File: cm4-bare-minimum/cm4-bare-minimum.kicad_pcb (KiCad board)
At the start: 2 copper layers, 120 x 40 mm, 24 parts, among them J1 Micro_SD_Card_Det, J2 690-019-298-412, J3 THD-02-R, J4 USB4105-GF-A, J5 USB_OTG, U1 RT9742GGJ5, U2 RT9742SNGV, U3 FSUSB42MUX, U5 MagJack-A70-112-331N126

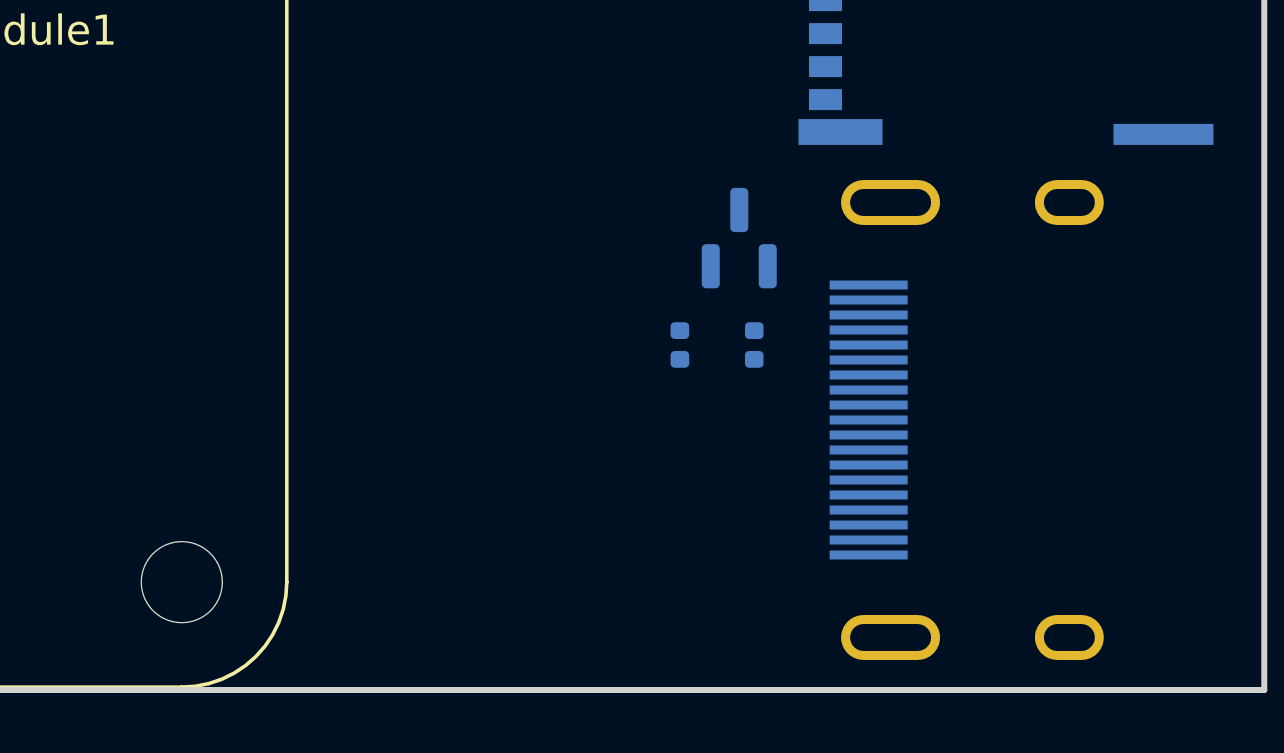
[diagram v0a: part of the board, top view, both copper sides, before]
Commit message: Connector changed, Added Labels.
Changed HDMI connector to upright. Added labels for included components in schematic.
To Do: Create tracks in PCB Layout. Add jumper for wifi bluetooth signals.
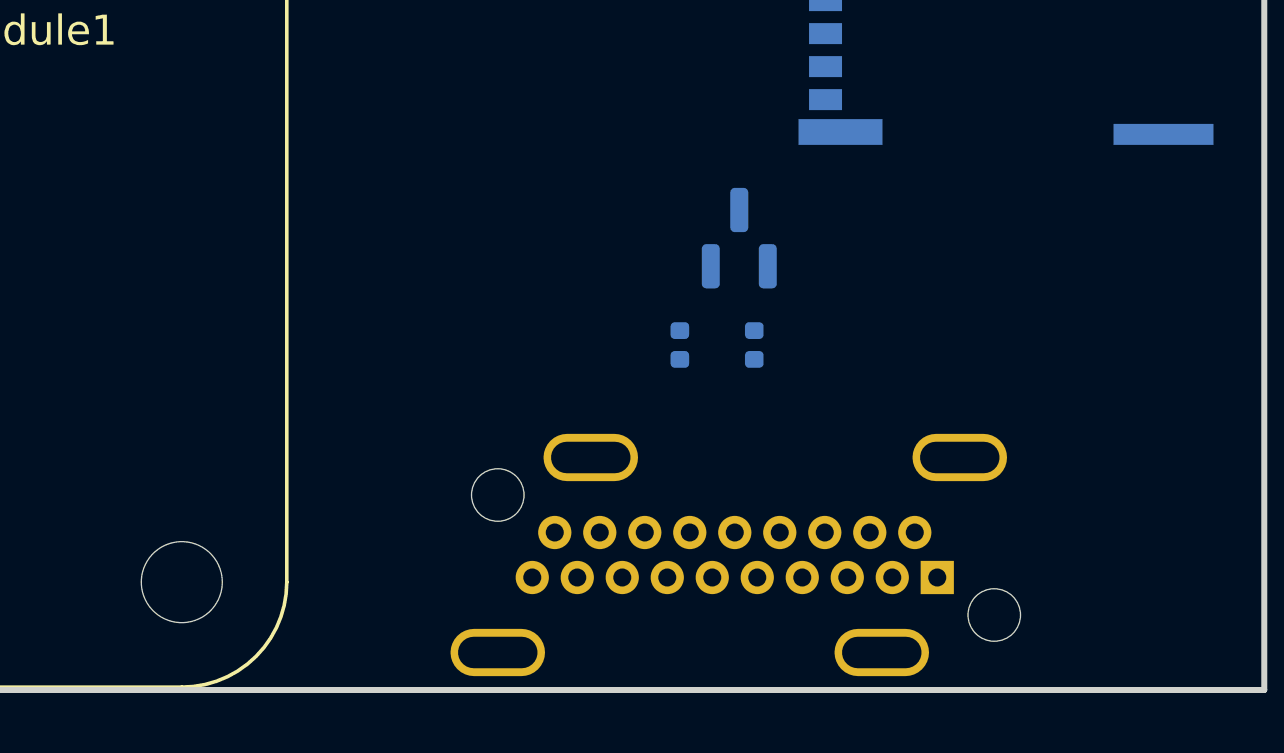
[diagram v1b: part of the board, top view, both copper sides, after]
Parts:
- removed J2: 690-019-298-412, CM4IO:EDAC 690-019-298-412
- added J6: G45A19170083HR, G45A19170083HR:AMPHENOL_G45A19170083HR, B.Cu at (201.5, 115.0)

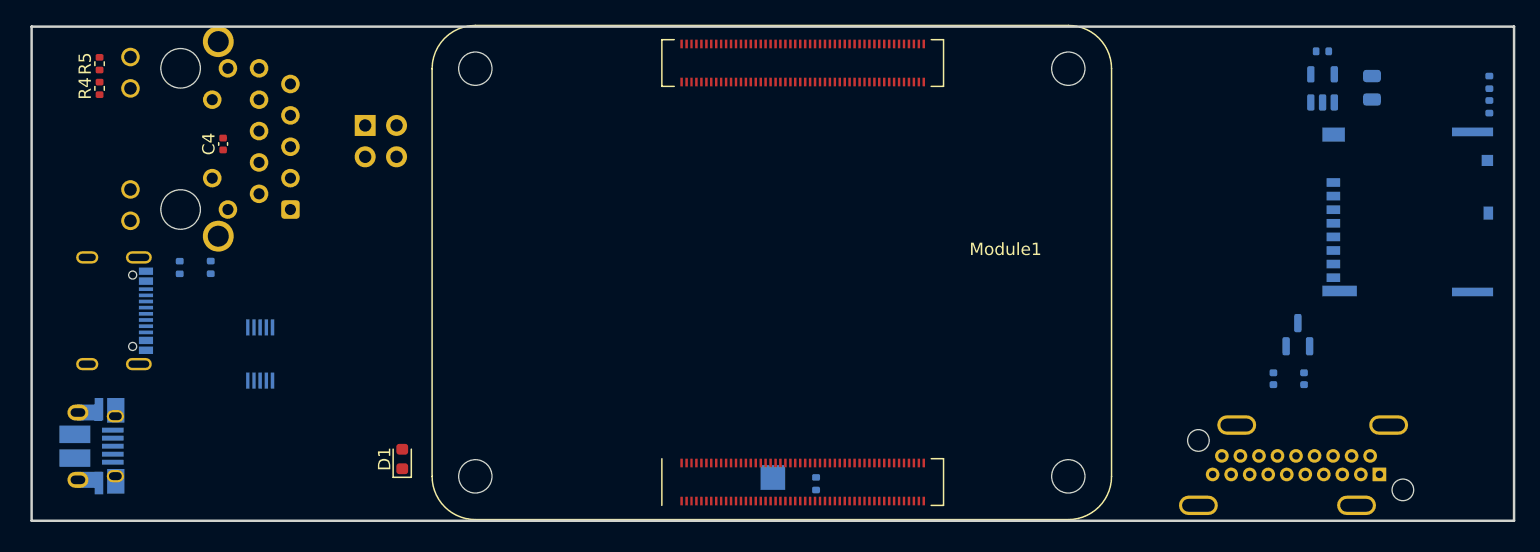
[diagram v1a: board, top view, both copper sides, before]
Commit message: updated V1 bare minimum board
Initiated pcb layout for V1 board
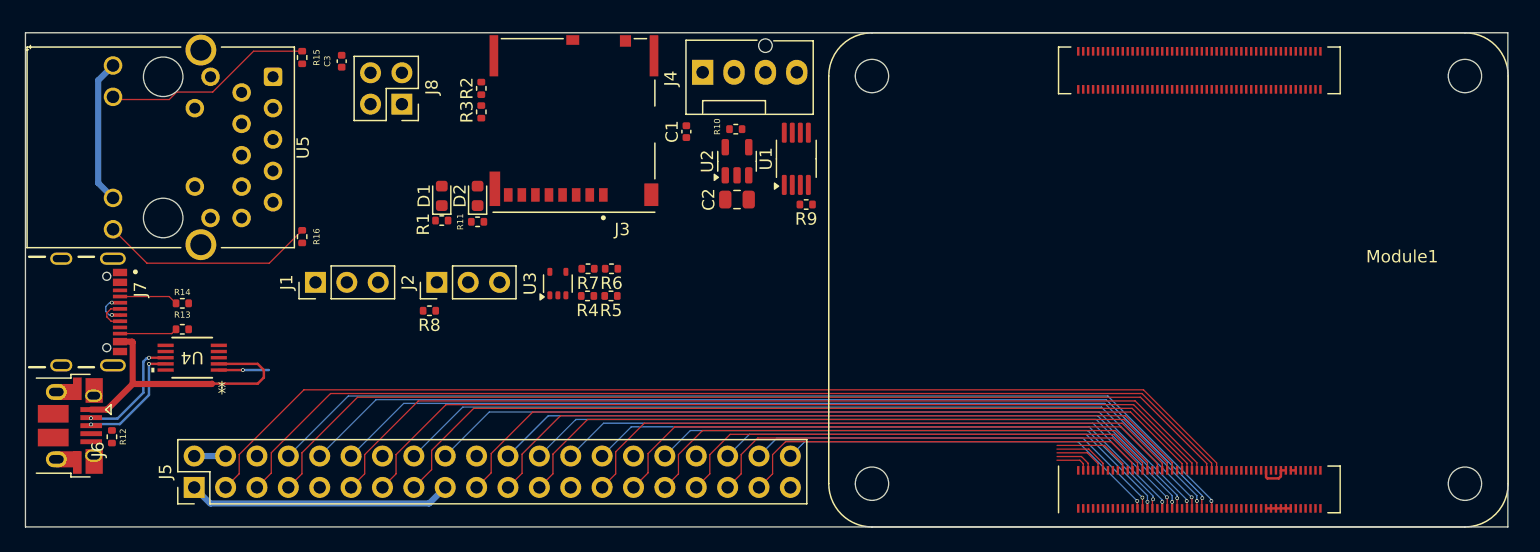
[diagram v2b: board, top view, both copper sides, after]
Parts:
- removed C4: 100n, Capacitor_SMD:C_0402_1005Metric
- removed TP1: TestPoint, TestPoint:TestPoint_Pad_2.0x2.0mm
- added D2: LED Red, LED_SMD:LED_0603_1608Metric, F.Cu at (126.6, 93.2)
- added J2: Conn_01x03, Connector_PinHeader_2.54mm:PinHeader_1x03_P2.54mm_Vertical, F.Cu at (123.3, 100.2)
- added J7: USB4105-GF-A, USB4105-GF-A:GCT_USB4105-GF-A, F.Cu at (92.9, 102.6)
- added J8: THD-02-R, Connector_PinHeader_2.54mm:PinHeader_2x02_P2.54mm_Vertical, F.Cu at (120.5, 85.8)
- added R10: 12K 1%, Resistor_SMD:R_0402_1005Metric, F.Cu at (147.5, 87.8)
- added R11: 1k, Resistor_SMD:R_0402_1005Metric, F.Cu at (126.6, 95.3)
- added R12: 2.2K 1%, Resistor_SMD:R_0402_1005Metric, F.Cu at (97.0, 112.7)
- added R13: 5.1k, Resistor_SMD:R_0402_1005Metric, F.Cu at (102.7, 104.0)
- added R14: 5.1k, Resistor_SMD:R_0402_1005Metric, F.Cu at (102.7, 101.9)
- added R15: 470R, Resistor_SMD:R_0402_1005Metric, F.Cu at (112.4, 82.0)
- added R16: 470R, Resistor_SMD:R_0402_1005Metric, F.Cu at (112.4, 96.5)
- added R9: 36K 1%, Resistor_SMD:R_0402_1005Metric, F.Cu at (153.2, 93.9)
- added U4: FSUSB42MUX, FSUSB42MUX:MSOP10_3X3_ONS, F.Cu at (103.5, 106.3)
- C1: value 10u -> 100n; footprint Capacitor_SMD:C_0805_2012Metric -> Capacitor_SMD:C_0402_1005Metric; moved to F.Cu
- C2: value 100n -> 10u; footprint Capacitor_SMD:C_0402_1005Metric -> Capacitor_SMD:C_0805_2012Metric; moved to F.Cu
- C3, U5: moved to F.Cu
- J1: value Micro_SD_Card_Det -> Conn_01x03; footprint CM4IO:SDCARD_MOLEX_503398-1892 -> Connector_PinHeader_2.54mm:PinHeader_1x03_P2.54mm_Vertical; moved to F.Cu
- J3: value THD-02-R -> Micro_SD_Card_Det; footprint Connector_PinHeader_2.54mm:PinHeader_2x02_P2.54mm_Vertical -> CM4IO:SDCARD_MOLEX_503398-1892; moved to F.Cu
- J4: value USB4105-GF-A -> Molex 470531000; footprint USB4105-GF-A:GCT_USB4105-GF-A -> Connector:FanPinHeader_1x04_P2.54mm_Vertical; moved to F.Cu
- J5: value USB_OTG -> THD-20-R; footprint CM4IO:USB_Micro-B_EDAC_UCON00686 -> Connector_PinHeader_2.54mm:PinHeader_2x20_P2.54mm_Vertical; moved to F.Cu
- J6: value G45A19170083HR -> USB_OTG; footprint G45A19170083HR:AMPHENOL_G45A19170083HR -> CM4IO:USB_Micro-B_EDAC_UCON00686; moved to F.Cu
- R1: value nf -> 1k; moved to F.Cu
- R2: value nf -> NC; moved to F.Cu
- R3: value 12K 1% -> NC; moved to F.Cu
- R4, R5: value 470R -> NC
- R6: value 1k -> NC; moved to F.Cu
- R7: value 2.2K 1% -> NC; moved to F.Cu
- R8: value 5.1k -> NC; moved to F.Cu
- U1: value RT9742GGJ5 -> EMC2301-1-ACZL-TR; footprint Package_TO_SOT_SMD:SOT-23-5 -> Package_SO:MSOP-8_3x3mm_P0.65mm; moved to F.Cu
- U2: value RT9742SNGV -> RT9742GGJ5; footprint Package_TO_SOT_SMD:SOT-23 -> Package_TO_SOT_SMD:SOT-23-5; moved to F.Cu
- U3: value FSUSB42MUX -> 74LVC1G07SE-7; footprint FSUSB42MUX:MSOP10_3X3_ONS -> Package_TO_SOT_SMD:SOT-353_SC-70-5; moved to F.Cu
- moved J6 109.0 mm to (92.5, 111.8)
- moved J1 88.2 mm to (113.5, 100.2), turned to 90 degrees
- moved R1 85.5 mm to (123.7, 95.2), turned to 0 degrees
- moved R2 81.6 mm to (126.9, 84.5)
- moved C3 79.7 mm to (115.6, 82.3)
- moved R3 68.3 mm to (126.9, 86.4), turned to 90 degrees
- moved C1 55.6 mm to (143.5, 88.0)
- moved J4 53.4 mm to (144.8, 83.2), turned to 0 degrees
- moved C2 48.1 mm to (147.6, 93.5), turned to 0 degrees
- moved U2 47.5 mm to (147.6, 90.4)
- moved R5 45.5 mm to (137.4, 101.3), turned to 180 degrees
- moved U1 43.0 mm to (152.4, 90.2)
- moved R4 42.9 mm to (135.5, 101.3), turned to 180 degrees
- moved Module1 32.1 mm to (210.0, 120.0)
- moved R7 30.5 mm to (135.5, 99.1), turned to 180 degrees
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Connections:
- C1 pad 1: /SD_PWR -> /CM4_3V3
- C2 pad 1: /CM4_5V -> /SD_PWR
- C3 pad 1: /HDMI_5v -> Net-(C3-Pad1)
- J1 pad 1: /SD_DAT2 -> /Global_EN
- J1 pad 2: /SD_DAT3 -> GND
- J1 pad 3: /SD_CMD -> /RUN_PG
- J3 pad 1: /TR1_TAP -> /SD_DAT2
- J3 pad 2: /TR2_TAP -> /SD_DAT3
- J3 pad 3: /TR0_TAP -> /SD_CMD
- J3 pad 4: /TR3_TAP -> /SD_PWR
- J5 pad 1: /USB_OTG_ID -> /CM4_3V3
- J5 pad 2: /USB_D_N -> /CM4_5V
- J5 pad 3: /USB_D_P -> /GPIO2
- J5 pad 4: unconnected-(J5-ID-Pad4) -> /CM4_5V
- J5 pad 5: GND -> /GPIO3
- J6 pad 1: /HDMI0_D2_P -> /USB_OTG_ID
- J6 pad 2: GND -> /USB_D_N
- J6 pad 3: /HDMI0_D2_N -> /USB_D_P
- J6 pad 4: /HDMI0_D1_P -> unconnected-(J6-ID-Pad4)
- J6 pad 6: /HDMI0_D1_N -> GND
- Module1 pad 100: /nEXTRST -> unconnected-(Module1A-nEXTRST-Pad100)
- Module1 pad 111: /VDAC_COMP -> unconnected-(Module1B-VDAC_COMP-Pad111)
- Module1 pad 15: GND -> /ETH_LEDY
- Module1 pad 151: /HDMI0_CEC -> unconnected-(Module1B-HDMI0_CEC-Pad151)
- Module1 pad 153: /HDMI0_HOTPLUG -> unconnected-(Module1B-HDMI0_HOTPLUG-Pad153)
- Module1 pad 17: GND -> /ETH_LEDG
- Module1 pad 170: /HDMI0_D2_P -> unconnected-(Module1B-HDMI0_TX2_P-Pad170)
- Module1 pad 172: /HDMI0_D2_N -> unconnected-(Module1B-HDMI0_TX2_N-Pad172)
- Module1 pad 176: /HDMI0_D1_P -> unconnected-(Module1B-HDMI0_TX1_P-Pad176)
- Module1 pad 178: /HDMI0_D1_N -> unconnected-(Module1B-HDMI0_TX1_N-Pad178)
- Module1 pad 182: /HDMI0_D0_P -> unconnected-(Module1B-HDMI0_TX0_P-Pad182)
- Module1 pad 184: /HDMI0_D0_N -> unconnected-(Module1B-HDMI0_TX0_N-Pad184)
- Module1 pad 188: /HDMI0_CK_P -> unconnected-(Module1B-HDMI0_CLK_P-Pad188)
- Module1 pad 190: /HDMI0_CK_N -> unconnected-(Module1B-HDMI0_CLK_N-Pad190)
- Module1 pad 199: /HDMI0_SDA -> unconnected-(Module1B-HDMI0_SDA-Pad199)
- Module1 pad 200: /HDMI0_SCL -> unconnected-(Module1B-HDMI0_SCL-Pad200)
- Module1 pad 24: unconnected-(Module1A-GPIO26-Pad24) -> /GPIO26
- Module1 pad 25: unconnected-(Module1A-GPIO21-Pad25) -> /GPIO21
- Module1 pad 26: unconnected-(Module1A-GPIO19-Pad26) -> /GPIO19
- Module1 pad 27: unconnected-(Module1A-GPIO20-Pad27) -> /GPIO20
- Module1 pad 28: unconnected-(Module1A-GPIO13-Pad28) -> /GPIO13
- Module1 pad 29: unconnected-(Module1A-GPIO16-Pad29) -> /GPIO16
- Module1 pad 30: unconnected-(Module1A-GPIO6-Pad30) -> /GPIO6
- Module1 pad 31: unconnected-(Module1A-GPIO12-Pad31) -> /GPIO12
- Module1 pad 34: unconnected-(Module1A-GPIO5-Pad34) -> /GPIO5
- Module1 pad 35: unconnected-(Module1A-ID_SC-Pad35) -> /ID_SC
- Module1 pad 36: unconnected-(Module1A-ID_SD-Pad36) -> /ID_SD
- Module1 pad 37: unconnected-(Module1A-GPIO7-Pad37) -> /GPIO7
- Module1 pad 38: unconnected-(Module1A-GPIO11-Pad38) -> /GPIO11
- Module1 pad 39: unconnected-(Module1A-GPIO8-Pad39) -> /GPIO8
- Module1 pad 40: unconnected-(Module1A-GPIO9-Pad40) -> /GPIO9
- Module1 pad 41: unconnected-(Module1A-GPIO25-Pad41) -> /GPIO25
- Module1 pad 44: unconnected-(Module1A-GPIO10-Pad44) -> /GPIO10
- Module1 pad 45: unconnected-(Module1A-GPIO24-Pad45) -> /GPIO24
- Module1 pad 46: unconnected-(Module1A-GPIO22-Pad46) -> /GPIO22
- Module1 pad 47: unconnected-(Module1A-GPIO23-Pad47) -> /GPIO23
- Module1 pad 48: unconnected-(Module1A-GPIO27-Pad48) -> /GPIO27
- Module1 pad 49: unconnected-(Module1A-GPIO18-Pad49) -> /GPIO18
- Module1 pad 50: unconnected-(Module1A-GPIO17-Pad50) -> /GPIO17
- Module1 pad 51: unconnected-(Module1A-GPIO15-Pad51) -> /GPIO15
- Module1 pad 54: unconnected-(Module1A-GPIO4-Pad54) -> /GPIO4
- Module1 pad 55: unconnected-(Module1A-GPIO14-Pad55) -> /GPIO14
- Module1 pad 56: unconnected-(Module1A-GPIO3-Pad56) -> /GPIO3
- Module1 pad 58: unconnected-(Module1A-GPIO2-Pad58) -> /GPIO2
- Module1 pad 73: unconnected-(Module1A-SD_VDD_Override-Pad73) -> /SD_VDD_Override
- Module1 pad 78: unconnected-(Module1A-GPIO_VREF(1.8v/3.3v_Input)-Pad78) -> /CM4_3V3
- Module1 pad 80: unconnected-(Module1A-SCL0-Pad80) -> /SCL0
- Module1 pad 82: unconnected-(Module1A-SDA0-Pad82) -> /SDA0
- Module1 pad 94: unconnected-(Module1A-AnalogIP1-Pad94) -> /AnalogIP1
- Module1 pad 96: unconnected-(Module1A-AnalogIP0-Pad96) -> /AnalogIP0
- R1 pad 1: /CM4_3V3 -> Net-(D1-K)
- R1 pad 2: Net-(J1-DET_A) -> Net-(Module1A-PI_nLED_Activity)
- R2 pad 1: unconnected-(R2-Pad1) -> /CM4_3V3
- R2 pad 2: Net-(J1-DET_B) -> Net-(J3-DET_A)
- R3 pad 1: /CM4_3V3 -> /Reserved
- R3 pad 2: /SD_PWR_ON -> Net-(J3-DET_B)
- R4 pad 1: Net-(U5-LEDG_K) -> /SD_VDD_Override
- R5 pad 1: Net-(U5-LEDY_K) -> /EEPROM_nWP
- R6 pad 1: Net-(D1-K) -> /BT_nDisable
- R6 pad 2: Net-(Module1A-PI_nLED_Activity) -> GND
- R7 pad 1: /USB_OTG_ID -> /WiFi_nDisable
- R8 pad 1: Net-(J4-CC1) -> Net-(J2-Pin_1)
- R8 pad 2: GND -> /CM4_3V3
- U1 pad 1: /SD_PWR -> /SDA0
- U1 pad 2: GND -> /SCL0
- U1 pad 3: unconnected-(U1-nFLG-Pad3) -> /CM4_3V3
- U1 pad 4: /SD_PWR_ON -> GND
- U1 pad 5: /CM4_3V3 -> Net-(J4-Pin_4)
- U2 pad 1: /CM4_5V -> /SD_PWR
- U2 pad 2: /HDMI_5v -> GND
- U2 pad 3: GND -> unconnected-(U2-nFLG-Pad3)
- U3 pad 1: /CM4_3V3 -> (no net)
- U3 pad 2: /USB_OTG_ID -> /nPI_LED_PWR
- U3 pad 3: /USB2_P -> GND
- U3 pad 4: /USB2_N -> Net-(R11-Pad2)
- U3 pad 5: GND -> /CM4_3V3
- U5 pad 1: /TRD0_P -> unconnected-(U5-TRD0+-Pad1)
- U5 pad 4: Net-(C4-Pad1) -> Net-(C3-Pad1)
- U5 pad 5: Net-(C4-Pad1) -> Net-(C3-Pad1)
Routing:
- net /GPIO2: track 0.00 -> 87.5 mm
- net /GPIO3: track 0.00 -> 84.3 mm
- net /GPIO4: track 0.00 -> 81.1 mm
- net /GPIO14: track 0.00 -> 80.9 mm, vias 0 -> 1
- net /GPIO15: track 0.00 -> 77.6 mm, vias 0 -> 1
- net /GPIO17: track 0.00 -> 75.0 mm
- net /GPIO18: track 0.00 -> 74.4 mm, vias 0 -> 1
- net /GPIO27: track 0.00 -> 71.8 mm
- net /GPIO22: track 0.00 -> 68.6 mm
- net /GPIO23: track 0.00 -> 68.5 mm, vias 0 -> 1
- net /GPIO24: track 0.00 -> 65.2 mm, vias 0 -> 1
- net /GPIO10: track 0.00 -> 62.8 mm
- net /GPIO9: track 0.00 -> 59.3 mm
- net /GPIO25: track 0.00 -> 59.3 mm, vias 0 -> 1
- net /GPIO11: track 0.00 -> 56.1 mm
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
